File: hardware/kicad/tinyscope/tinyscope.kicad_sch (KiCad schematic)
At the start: 65 parts, among them J1 USB_C_Receptacle_USB2.0, J2 Conn_01x02, J3 Conn_01x02, Q1 PMOS, U1 USBLC6-2SC6_MOD, U2 BQ24075RGT, U3 MAX17048G, U4 TPS54360DDA, U5 TPS63802DLAR, U6 TPS63802DLAR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

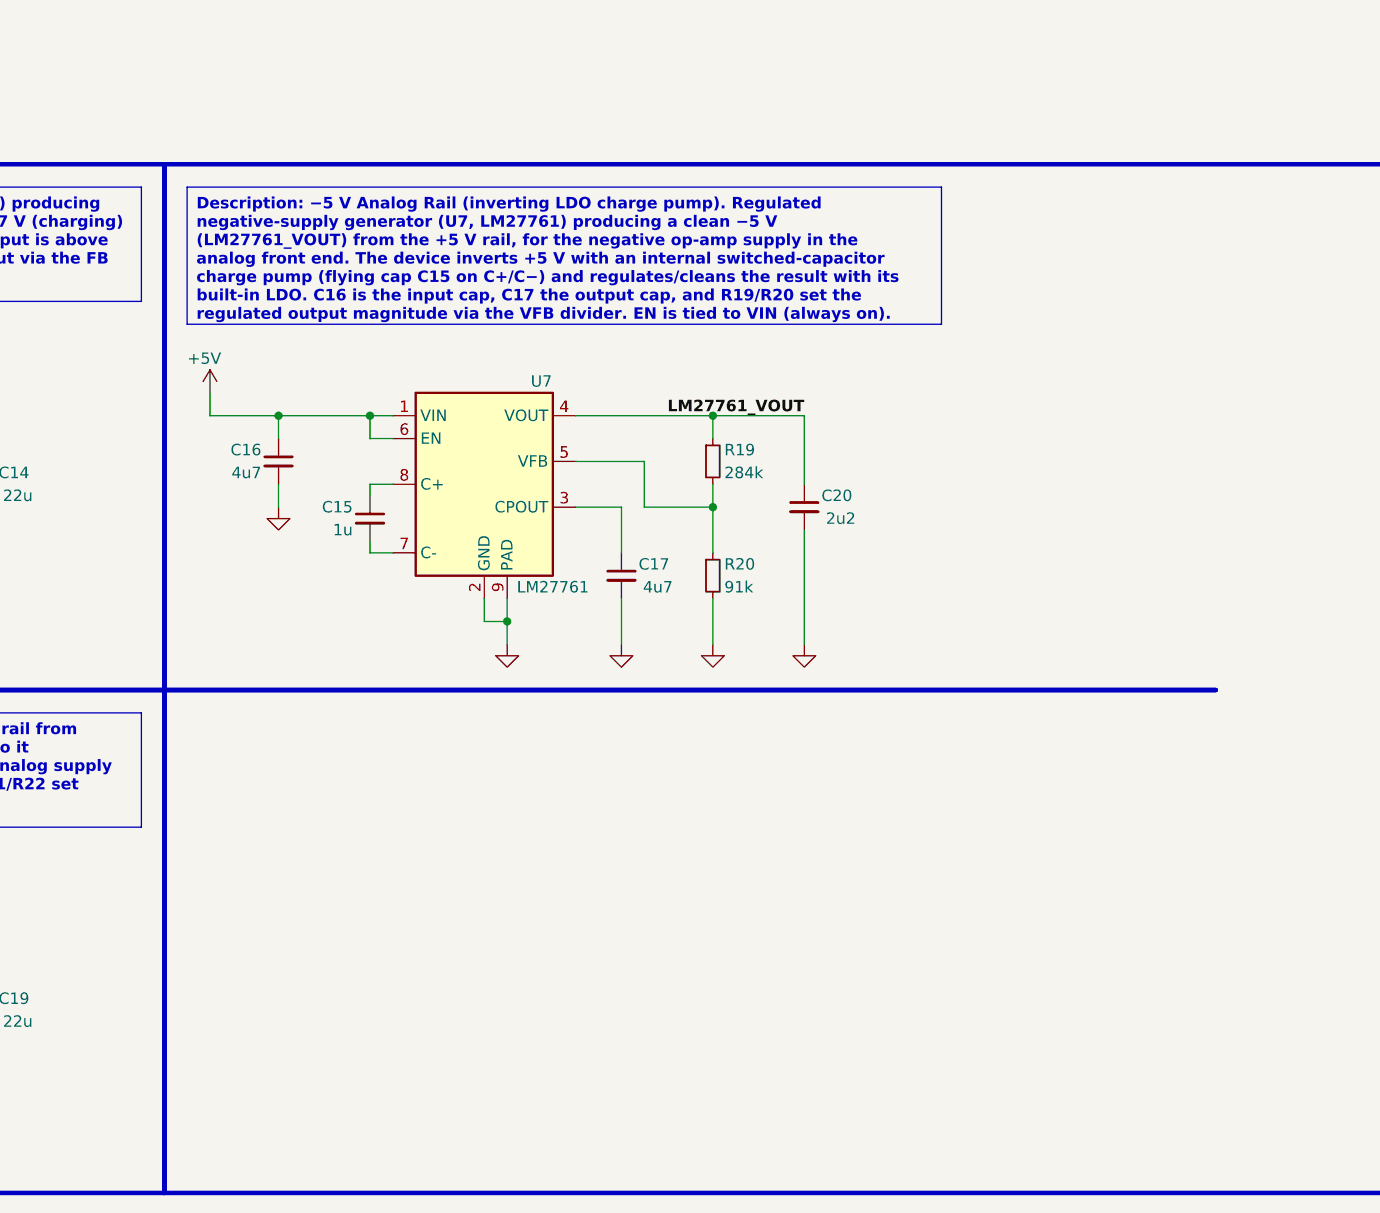
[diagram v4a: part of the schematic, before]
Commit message: feat: hardware: Add tinyscope kicad project. Adds REF3030 Voltage Reference 3.0V
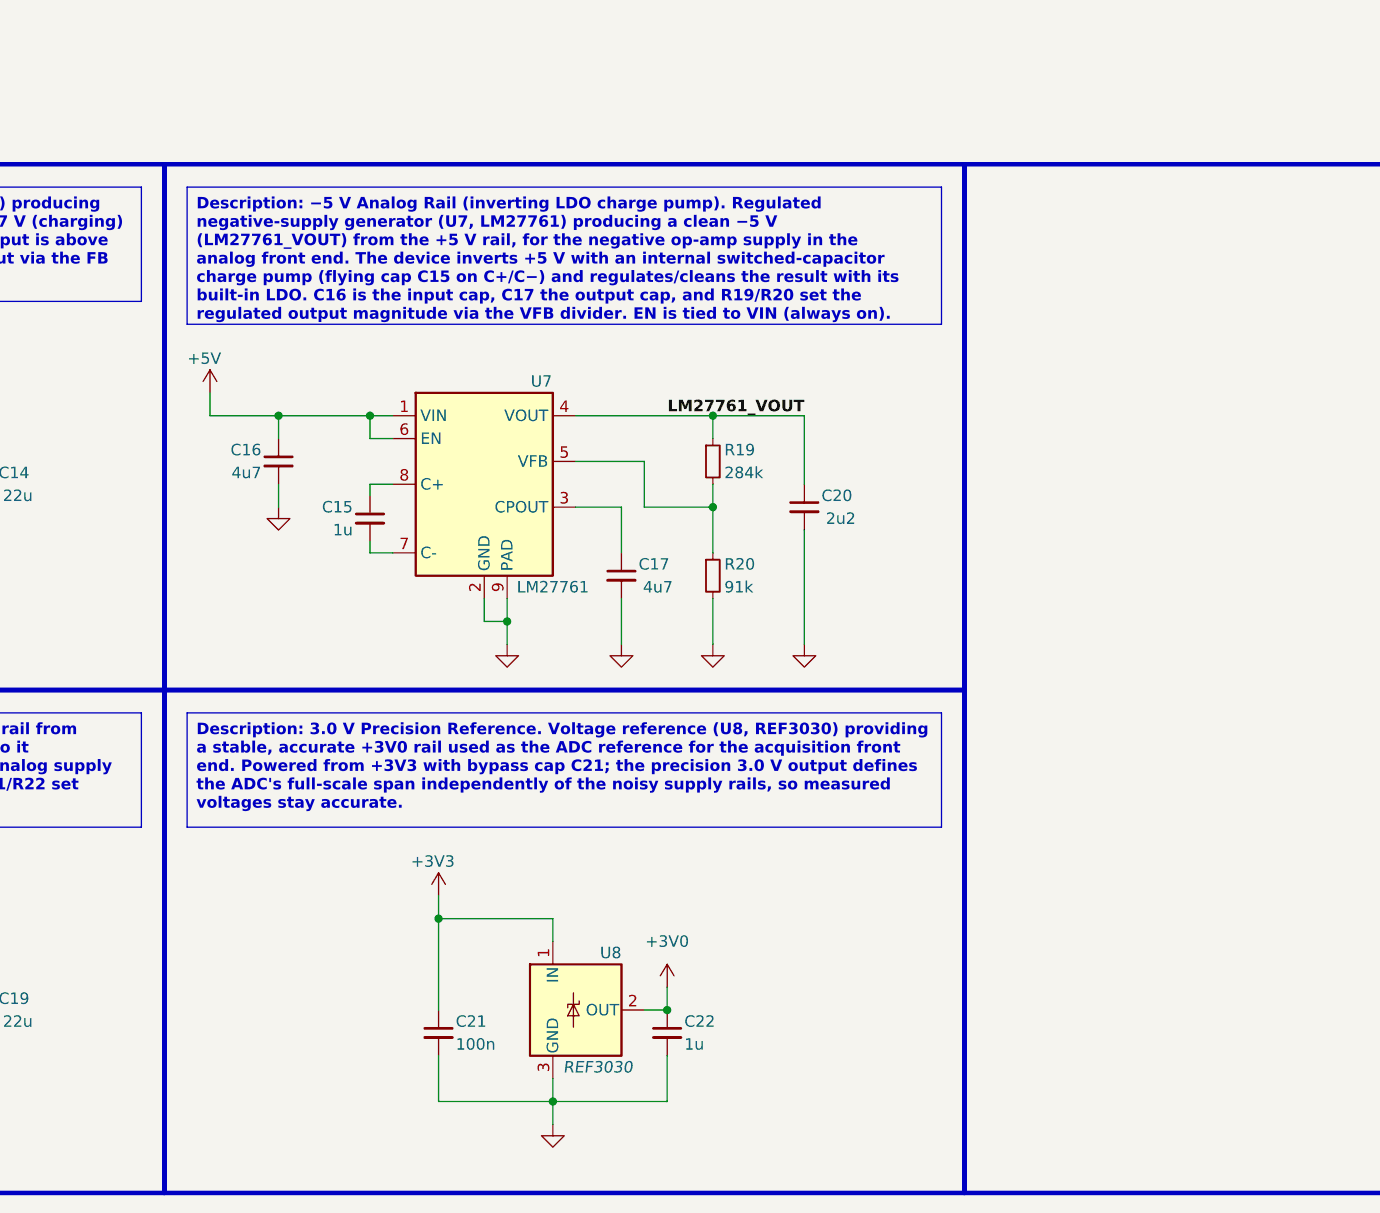
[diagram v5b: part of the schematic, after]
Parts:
- added C21: 100n, symbol Device:C_Small
- added C22: 1u, symbol Device:C_Small
- added U8: REF3030, Package_TO_SOT_SMD:SOT-23, symbol Reference_Voltage:REF3030
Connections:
- net +3V3: now also C21.1, U8.1 (IN)
- net GND: now also C21.2, C22.2, U8.3 (GND)
- new net +3V0: C22.1, U8.2 (OUT)
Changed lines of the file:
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@@
   (junction (at 96.52 48.26) (diameter 0) (color 0 0 0 0)
   )
+  (junction (at 195.58 254) (diameter 0) (color 0 0 0 0)
+  )
   (junction (at 218.44 50.8) (diameter 0) (color 0 0 0 0)
   )
@@
   (junction (at 119.38 190.5) (diameter 0) (color 0 0 0 0)
   )
+  (junction (at 182.88 264.16) (diameter 0) (color 0 0 0 0)
+  )
   (junction (at 96.52 50.8) (diameter 0) (color 0 0 0 0)
   )
@@
   (junction (at 58.42 256.54) (diameter 0) (color 0 0 0 0)
   )
+  (junction (at 170.18 243.84) (diameter 0) (color 0 0 0 0)
+  )
   (junction (at 71.12 238.76) (diameter 0) (color 0 0 0 0)
   )
@@
     (stroke (width 0) (type default))
   )
+  (wire (pts (xy 195.58 264.16) (xy 182.88 264.16))
+    (stroke (width 0) (type default))
+  )
   (wire (pts (xy 66.04 73.66) (xy 73.66 73.66))
     (stroke (width 0) (type default))
@@
     (stroke (width 0) (type default))
   )
+  (wire (pts (xy 195.58 251.46) (xy 195.58 254))
+    (stroke (width 0) (type default))
+  )
   (wire (pts (xy 218.44 73.66) (xy 228.6 73.66))
     (stroke (width 0) (type default))
@@
     (stroke (width 0) (type default))
   )
+  (wire (pts (xy 170.18 259.08) (xy 170.18 264.16))
+    (stroke (width 0) (type default))
+  )
   (wire (pts (xy 180.34 101.6) (xy 182.88 101.6))
     (stroke (width 0) (type default))
@@
     (stroke (width 0) (type default))
   )
+  (wire (pts (xy 195.58 259.08) (xy 195.58 264.16))
+    (stroke (width 0) (type default))
+  )
   (wire (pts (xy 71.12 180.34) (xy 71.12 190.5))
     (stroke (width 0) (type default))
@@
     (stroke (width 0) (type default))
   )
+  (wire (pts (xy 170.18 243.84) (xy 182.88 243.84))
+    (stroke (width 0) (type default))
+  )
   (wire (pts (xy 104.14 190.5) (xy 119.38 190.5))
     (stroke (width 0) (type default))
@@
     (stroke (width 0) (type default))
   )
+  (wire (pts (xy 182.88 243.84) (xy 182.88 246.38))
+    (stroke (width 0) (type default))
+  )
   (wire (pts (xy 241.3 55.88) (xy 241.3 58.42))
     (stroke (width 0) (type default))
@@
     (stroke (width 0) (type default))
   )
+  (wire (pts (xy 182.88 261.62) (xy 182.88 264.16))
+    (stroke (width 0) (type default))
+  )
   (wire (pts (xy 251.46 48.26) (xy 261.62 48.26))
     (stroke (width 0) (type default))
@@
     (stroke (width 0) (type default))
   )
+  (wire (pts (xy 170.18 243.84) (xy 170.18 254))
+    (stroke (width 0) (type default))
+  )
   (wire (pts (xy 101.6 200.66) (xy 106.68 200.66))
     (stroke (width 0) (type default))
@@
     (stroke (width 0) (type default))
   )
+  (wire (pts (xy 170.18 241.3) (xy 170.18 243.84))
+    (stroke (width 0) (type default))
+  )
   (wire (pts (xy 96.52 109.22) (xy 96.52 111.76))
     (stroke (width 0) (type default))
@@
     (stroke (width 0) (type default))
   )
+  (wire (pts (xy 193.04 254) (xy 195.58 254))
+    (stroke (width 0) (type default))
+  )
   (wire (pts (xy 119.38 246.38) (xy 119.38 248.92))
     (stroke (width 0) (type default))
@@
     (stroke (width 0) (type default))
   )
+  (wire (pts (xy 182.88 264.16) (xy 182.88 266.7))
+    (stroke (width 0) (type default))
+  )
   (wire (pts (xy 101.6 195.58) (xy 104.14 195.58))
     (stroke (width 0) (type default))
@@
     (stroke (width 0) (type default))
   )
+  (wire (pts (xy 170.18 264.16) (xy 182.88 264.16))
+    (stroke (width 0) (type default))
+  )
   (wire (pts (xy 302.26 104.14) (xy 317.5 104.14))
     (stroke (width 0) (type default))
@@
     (stroke (width 0) (type default))
   )
+  (rectangle (start 228.6 160.02) (end 228.6 274.32)
+    (stroke (width 0.5) (type default) (color 0 0 0 1))
+    (fill (type none))
+  )
   (rectangle (start 279.4 160.02) (end 398.78 233.68)
     (stroke (width 0.5) (type default) (color 0 0 0 1))
@@
     (fill (type none))
   )
-  (rectangle (start 139.7 218.44) (end 256.54 218.44)
+  (rectangle (start 139.7 218.44) (end 228.6 218.44)
     (stroke (width 0.5) (type default) (color 0 0 0 1))
     (fill (type none))
@@
     (effects (font (size 1.27 1.27) bold) (justify left top))
   )
+  (text_box "Description: 3.0 V Precision Reference. Voltage reference (U8, REF3030) providing a stable, accurate +3V0 rail used as the ADC reference for the acquisition front end. Powered from +3V3 with bypass cap C21; the precision 3.0 V output defines the ADC's full-scale span independently of the noisy supply rails, so measured voltages stay accurate."
+    (at 142.24 220.98 0) (size 83.82 12.7)
+    (stroke (width 0) (type default))
+    (fill (type color) (color 255 255 194 1))
+    (effects (font (size 1.27 1.27) bold) (justify left top))
+  )
   (text_box "Description: Battery / Power Connectors. Screw/JST terminals: J2 = EXT_BATT+ (the 12 V vehicle feed) and J3 = DEV_BATT+ (the lithium cell). Two distinct power sources, clearly separated.\n"
     (at 25.4 83.82 0) (size 111.76 7.62)
@@
     )
   )
+  (symbol (lib_id "Device:C_Small") (at 195.58 256.54 0) (unit 1)
+    (in_bom yes) (on_board yes) (dnp no)
+    (property "Reference" "C22" (at 197.485 255.27 0)
+      (effects (font (size 1.27 1.27)) (justify left))
+    )
+    (property "Value" "1u" (at 197.485 257.81 0)
+      (effects (font (size 1.27 1.27)) (justify left))
+    )
+    (property "Footprint" "" (at 195.58 256.54 0)
+      (effects (font (size 1.27 1.27)) hide)
+    )
+    (property "Datasheet" "~" (at 195.58 256.54 0)
+      (effects (font (size 1.27 1.27)) hide)
+    )
+    (pin "1")
+    (pin "2")
+    (instances
+      (project "tinyscope"
+        (path "/bb072e32-cc57-415a-8554-0e84d374f333"
+          (reference "C22") (unit 1)
+        )
+      )
+    )
+  )
   (symbol (lib_id "Device:C_Small") (at 210.82 198.12 0) (unit 1)
     (in_bom yes) (on_board yes) (dnp no)
@@
     )
   )
+  (symbol (lib_id "power:+3V3") (at 170.18 241.3 0) (unit 1)
+    (in_bom yes) (on_board yes) (dnp no)
+    (property "Reference" "#PWR038" (at 170.18 245.11 0)
+      (effects (font (size 1.27 1.27)) hide)
+    )
+    (property "Value" "+3V3" (at 169.545 237.49 0)
+      (effects (font (size 1.27 1.27)))
+    )
+    (property "Footprint" "" (at 170.18 241.3 0)
+      (effects (font (size 1.27 1.27)) hide)
+    )
+    (property "Datasheet" "" (at 170.18 241.3 0)
+      (effects (font (size 1.27 1.27)) hide)
+    )
+    (pin "1")
+    (instances
+      (project "tinyscope"
+        (path "/bb072e32-cc57-415a-8554-0e84d374f333"
+          (reference "#PWR038") (unit 1)
+        )
+      )
+    )
+  )
   (symbol (lib_id "TPS63802DLAR:TPS63802DLAR") (at 73.66 190.5 0) (unit 1)
     (in_bom yes) (on_board yes) (dnp no)
@@
     )
   )
+  (symbol (lib_id "power:+3V0") (at 195.58 251.46 0) (unit 1)
+    (in_bom yes) (on_board yes) (dnp no) (fields_autoplaced)
+    (property "Reference" "#PWR039" (at 195.58 255.27 0)
+      (effects (font (size 1.27 1.27)) hide)
+    )
+    (property "Value" "+3V0" (at 195.58 246.38 0)
+      (effects (font (size 1.27 1.27)))
+    )
+    (property "Footprint" "" (at 195.58 251.46 0)
+      (effects (font (size 1.27 1.27)) hide)
+    )
+    (property "Datasheet" "" (at 195.58 251.46 0)
+      (effects (font (size 1.27 1.27)) hide)
+    )
+    (pin "1")
+    (instances
+      (project "tinyscope"
+        (path "/bb072e32-cc57-415a-8554-0e84d374f333"
+          (reference "#PWR039") (unit 1)
+        )
+      )
+    )
+  )
   (symbol (lib_id "Device:C_Small") (at 228.6 68.58 0) (unit 1)
     (in_bom yes) (on_board yes) (dnp no)
@@
     )
   )
+  (symbol (lib_id "Reference_Voltage:REF3030") (at 185.42 254 0) (unit 1)
+    (in_bom yes) (on_board yes) (dnp no)
+    (property "Reference" "U8" (at 190.5 247.65 0)
+      (effects (font (size 1.27 1.27)) (justify right))
+    )
+    (property "Value" "REF3030" (at 191.77 260.35 0)
+      (effects (font (size 1.27 1.27) italic) (justify right))
+    )
+    (property "Footprint" "Package_TO_SOT_SMD:SOT-23" (at 185.42 265.43 0)
+      (effects (font (size 1.27 1.27) italic) hide)
+    )
+    (property "Datasheet" "http://www.ti.com/lit/ds/symlink/ref3033.pdf" (at 187.96 262.89 0)
+      (effects (font (size 1.27 1.27) italic) hide)
+    )
+    (pin "1")
+    (pin "2")
+    (pin "3")
+    (instances
+      (project "tinyscope"
+        (path "/bb072e32-cc57-415a-8554-0e84d374f333"
+          (reference "U8") (unit 1)
+        )
+      )
+    )
+  )
   (symbol (lib_id "Device:R_Small") (at 68.58 246.38 0) (unit 1)
     (in_bom yes) (on_board yes) (dnp no)
@@
     )
   )
+  (symbol (lib_id "power:GND") (at 182.88 266.7 0) (unit 1)
+    (in_bom yes) (on_board yes) (dnp no) (fields_autoplaced)
+    (property "Reference" "#PWR037" (at 182.88 273.05 0)
+      (effects (font (size 1.27 1.27)) hide)
+    )
+    (property "Value" "GND" (at 182.88 271.78 0)
+      (effects (font (size 1.27 1.27)) hide)
+    )
+    (property "Footprint" "" (at 182.88 266.7 0)
+      (effects (font (size 1.27 1.27)) hide)
+    )
+    (property "Datasheet" "" (at 182.88 266.7 0)
+      (effects (font (size 1.27 1.27)) hide)
+    )
+    (pin "1")
+    (instances
+      (project "tinyscope"
+        (path "/bb072e32-cc57-415a-8554-0e84d374f333"
+          (reference "#PWR037") (unit 1)
+        )
+      )
+    )
+  )
   (symbol (lib_id "power:+5V") (at 119.38 246.38 0) (unit 1)
     (in_bom yes) (on_board yes) (dnp no)
@@
         )
       )
+    )
+  )
+  (symbol (lib_id "Device:C_Small") (at 170.18 256.54 0) (unit 1)
+    (in_bom yes) (on_board yes) (dnp no)
+    (property "Reference" "C21" (at 172.085 255.27 0)
+      (effects (font (size 1.27 1.27)) (justify left))
+    )
+    (property "Value" "100n" (at 172.085 257.81 0)
+      (effects (font (size 1.27 1.27)) (justify left))
+    )
+    (property "Footprint" "" (at 170.18 256.54 0)
+      (effects (font (size 1.27 1.27)) hide)
+    )
+    (property "Datasheet" "~" (at 170.18 256.54 0)
+      (effects (font (size 1.27 1.27)) hide)
+    )
+    (pin "1")
+    (pin "2")
+    (instances
+      (project "tinyscope"
+        (path "/bb072e32-cc57-415a-8554-0e84d374f333"
+          (reference "C21") (unit 1)
+        )
+      )

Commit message: feat: hardware: Add tinyscope kicad project. Adds ADP742 low noise 5V LDO regulator
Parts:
- added C23, C24: 2u2, symbol Device:C_Small
- added C25: 1n, symbol Device:C_Small
- added U9: ADP7142, Package_SO:SOIC-8-1EP_3.9x4.9mm_P1.27mm_EP2.29x3mm, symbol Regulator_Linear:ADP7142ARDZ-5.0
- R21: value 806k -> 910k
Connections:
- net +5V: now also C24.1, U9.1 (VOUT), U9.2 (VOUT), U9.3 (SENSE/ADJ); no longer C19.1, R21.1, U6.6 (VOUT)
- net GND: now also C23.2, C24.2, C25.2, U9.4 (GND), U9.9 (GND)
- new net: C25.1, U9.6 (SS)
- new net TPS63802_VOUT: C19.1, C23.1, R21.1, U6.6 (VOUT), U9.5 (EN), U9.7 (VIN), U9.8 (VIN)
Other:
- moved on the sheet: C19

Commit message: feat: hardware: Add tinyscope kicad project. Divides project to subsheets. Adds power input and chargin sheet, regulation and rails sheet
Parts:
- removed C1, C15, C22: 1u, symbol Device:C_Small
- removed C10: 6800p, symbol Device:C_Small
- removed C11: 39p, symbol Device:C_Small
- removed C12, C13, C18: 10u, symbol Device:C_Small
- removed C14, C19: 22u, symbol Device:C_Small
- removed C16, C17, C2, C4: 4u7, symbol Device:C_Small
- removed C20, C23, C24, C5, C6: 2u2, symbol Device:C_Small
- removed C21, C3, C7: 100n, symbol Device:C_Small
- removed C25: 1n, symbol Device:C_Small
- removed C8, C9: 47u, symbol Device:C_Small
- removed D1, D2: LED_Small, symbol Device:LED_Small
- removed D3, D4: 0.3V, symbol Device:D_Schottky_Small
- removed D5: D_Small, symbol Device:D_Small
- removed D6: 15V, symbol Device:D_Zener_Small
- removed D7: D_TVS, symbol Device:D_TVS
- removed F1: 2A, symbol Device:Fuse_Small
- removed J1: USB_C_Receptacle_USB2.0, symbol Connector:USB_C_Receptacle_USB2.0
- removed J2, J3: Conn_01x02, symbol Connector_Generic:Conn_01x02
- removed L1: 8u2, symbol Device:L_Small
- removed L2, L4: 470n, symbol Device:L_Small
- removed Q1: PMOS, symbol Simulation_SPICE:PMOS
- removed R1, R2, R8: 5k1, symbol Device:R_Small
- removed R10: 84k5, symbol Device:R_Small
- removed R11: 162k, symbol Device:R_Small
- removed R12: 13k, symbol Device:R_Small
- removed R13: 59k4, symbol Device:R_Small
- removed R14: 10k2, symbol Device:R_Small
- removed R15, R18, R23: 100k, symbol Device:R_Small
- removed R16: 511k, symbol Device:R_Small
- removed R17, R20, R22: 91k, symbol Device:R_Small
- removed R19: 284k, symbol Device:R_Small
- removed R21: 910k, symbol Device:R_Small
- removed R3: 46k4, symbol Device:R_Small
- removed R4: 1k18, symbol Device:R_Small
- removed R5: 1k13, symbol Device:R_Small
- removed R6, R7: 1k5, symbol Device:R_Small
- removed R9: 523k, symbol Device:R_Small
- removed U1: USBLC6-2SC6_MOD, Package_TO_SOT_SMD:SOT-23-6, symbol Power_Protection:USBLC6-2SC6_MOD
- removed U2: BQ24075RGT, Package_DFN_QFN:VQFN-16-1EP_3x3mm_P0.5mm_EP1.6x1.6mm, symbol Battery_Management:BQ24075RGT
- removed U3: MAX17048G, SON50P200X200X80-9N-D, symbol MAX17048G+T10:MAX17048G+T10
- removed U4: TPS54360DDA, Package_SO:TI_SO-PowerPAD-8_ThermalVias, symbol Regulator_Switching:TPS54360DDA
- removed U5, U6: TPS63802DLAR, TPS63802DLAR, symbol TPS63802DLAR:TPS63802DLAR
- removed U7: LM27761, Package_SON:WSON-8-1EP_2x2mm_P0.5mm_EP0.9x1.6mm, symbol Regulator_SwitchedCapacitor:LM27761
- removed U8: REF3030, Package_TO_SOT_SMD:SOT-23, symbol Reference_Voltage:REF3030
- removed U9: ADP7142, Package_SO:SOIC-8-1EP_3.9x4.9mm_P1.27mm_EP2.29x3mm, symbol Regulator_Linear:ADP7142ARDZ-5.0
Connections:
- no-connect marks 2 -> 0
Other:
- added sheet MCUS (mcus.kicad_sch)
- added sheet Power Input & Charging (power_and_charging.kicad_sch)
- added sheet Regulation & Rails (regulation_and_rails.kicad_sch)
- note removed: "Power Input & Charging"
- note removed: "Regulation / Rails"
